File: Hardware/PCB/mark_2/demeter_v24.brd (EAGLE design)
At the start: 90 x 56 mm, 66 parts, among them IC1 4050, IC2 LM1117-5.0, IC3 LM1117-3.3, IC5 MCP3424, IC6 MCP23017SO, IC8 ATMEGA32U4-AU, Q1 IRLML6402, Q3 IRLML6402, Q5 IRLML6402

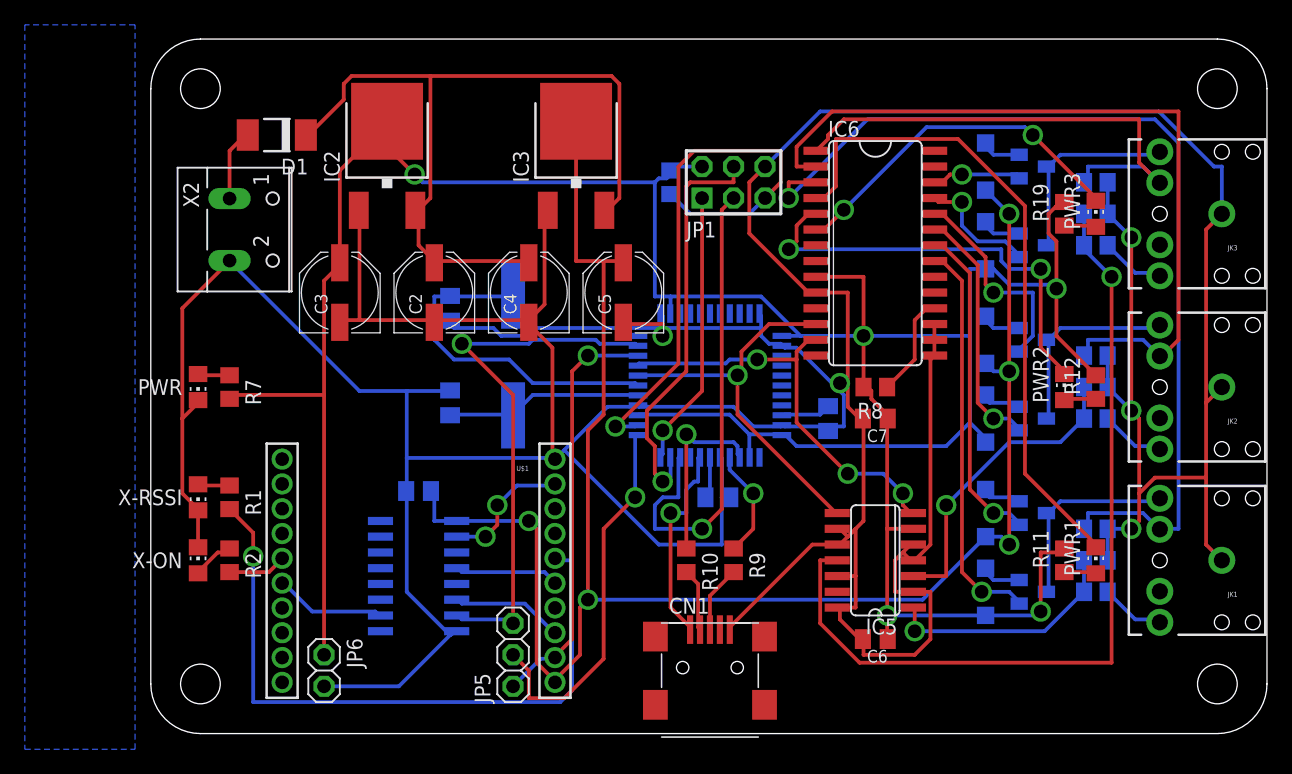
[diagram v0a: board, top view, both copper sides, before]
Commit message: 
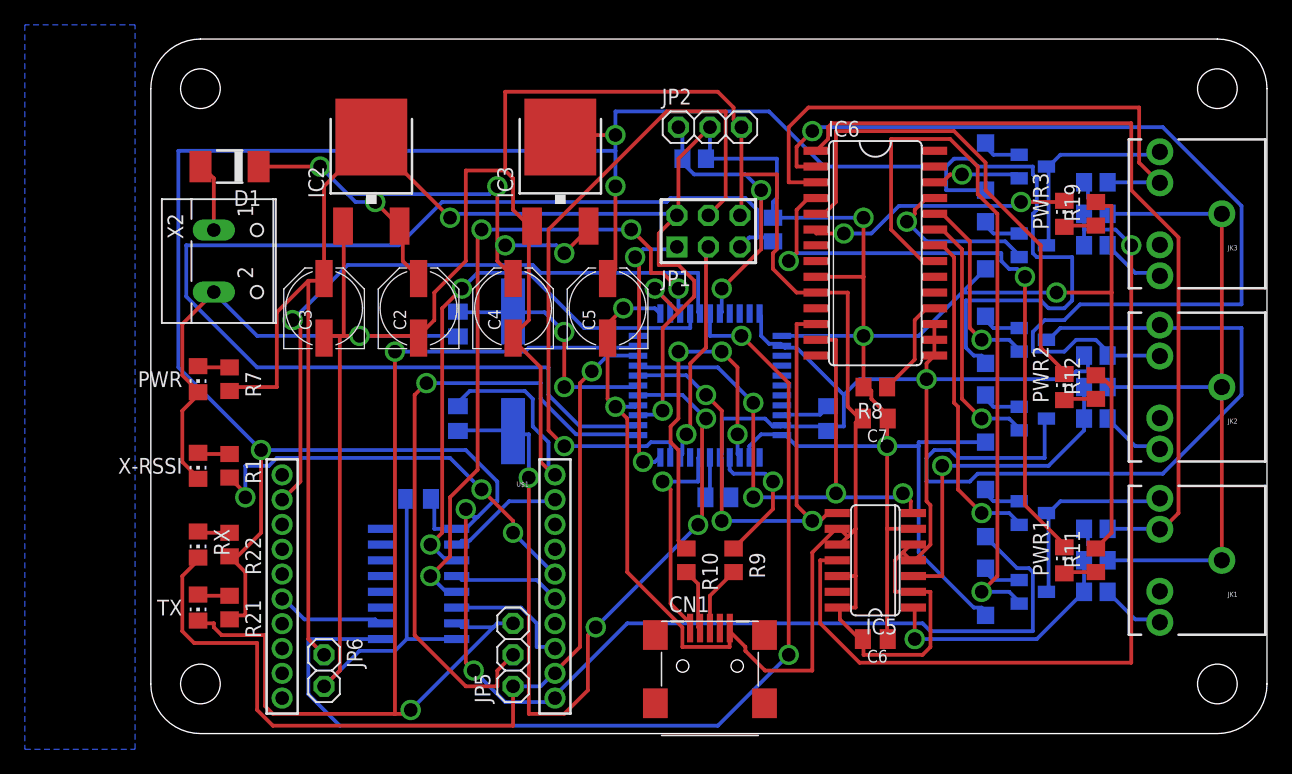
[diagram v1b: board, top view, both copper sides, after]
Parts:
- removed R2: (no value), mark_2:R0805
- removed X-ON: (no value), mark_2:CHIP-LED0805
- added JP2: (no value), mark_2:1X03
- added R20: 10k, mark_2:R0805
- added R21, R22: (no value), mark_2:R0805
- added RX, TX: (no value), mark_2:CHIP-LED0805
- moved R3 9.09 mm to (51.4, 41.9)
- moved D1 4.58 mm to (7.62, 47.0)
- moved JP1 4.43 mm to (46.2, 41.8)
- moved X2 2.84 mm to (7.62, 39.4)
- moved R1 2.54 mm to (7.62, 22.9)
- moved X-RSSI 2.54 mm to (5.08, 22.9)
- moved PWR1 2.54 mm to (74.9, 15.2)
- moved PWR3 2.54 mm to (74.9, 43.2)
- moved R11 2.54 mm to (77.5, 15.2)
- moved R19 2.54 mm to (77.5, 43.2)
- moved IC3 1.80 mm to (34.3, 47.0)
- moved C3 1.80 mm to (15.2, 35.6)
- moved C2 1.80 mm to (22.9, 35.6)
- moved C4 1.80 mm to (30.5, 35.6)
- moved IC2 1.80 mm to (19.1, 47.0)
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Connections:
- removed net CH4: IC5.13
- removed net N$10: R2.2, U$1.15
- removed net N$9: R2.1, X-ON.A
- new net DATA: IC8.29, JP2.1, R20.1
- new net N$36: R21.1, TX.A
- new net N$37: R22.1, RX.A
- new net RXLED: IC8.8
- new net TXLED: IC8.22
- net +3V3: now also R21.2, R22.2
- net +5V: now also JP2.2, R20.2
- net CTS: now also IC8.27
- net DTR: now also IC8.26
- net GND: now also JP2.3; no longer X-ON.C
- net RESET: now also IC8.25
- net RTS: now also IC8.28
- net RX: now also RX.C
- net SN1: now also IC6.1; no longer IC6.3
- net SN3: now also IC6.3; no longer IC6.1
- net TX: now also TX.C
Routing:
- net +3V3: track 142.7 -> 271.6 mm
- net RTS: track 0.00 -> 84.1 mm, vias 0 -> 2
- net CTS: track 0.00 -> 53.5 mm, vias 0 -> 1
- net RESET: track 0.00 -> 53.3 mm, vias 0 -> 4
- net RST: track 46.8 -> 99.7 mm, vias 1 -> 0
- net N$27: track 15.9 -> 66.3 mm, vias 0 -> 4
- net N$15: track 16.2 -> 65.4 mm
- net DTR: track 0.00 -> 46.3 mm, vias 0 -> 2
- net TX: track 43.6 -> 87.5 mm, vias 1 -> 2
- net RX: track 33.8 -> 76.2 mm
- net +5V: track 246.8 -> 282.5 mm, vias 5 -> 7
- net EN1-5: track 32.1 -> 58.7 mm
- net DATA: track 0.00 -> 22.0 mm, vias 0 -> 2
- net MOSI: track 33.5 -> 55.1 mm
- net EN: track 30.8 -> 51.7 mm
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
